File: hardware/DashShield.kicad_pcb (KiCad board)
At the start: 2 copper layers, 95 parts, among them J1 GPIO, J2 Steering Wheel, J3 Dash LEDs, J4 CAN0, J5 PWR, J7 CAN1, Q1 2N7002, Q2 2N7002, Q3 2N7002, Q4 2N7002, Q5 2N7002, Q6 2N7002, Q7 2N7002, Q8 2N7002, Q9 2N7002, U1 CAT24C256, U2 MCP2562-E-SN, U3 MCP2515-xST, U4 MCP2515-xST, U5 MCP2562-E-SN, Y1 8MHz, Y2 8MHz

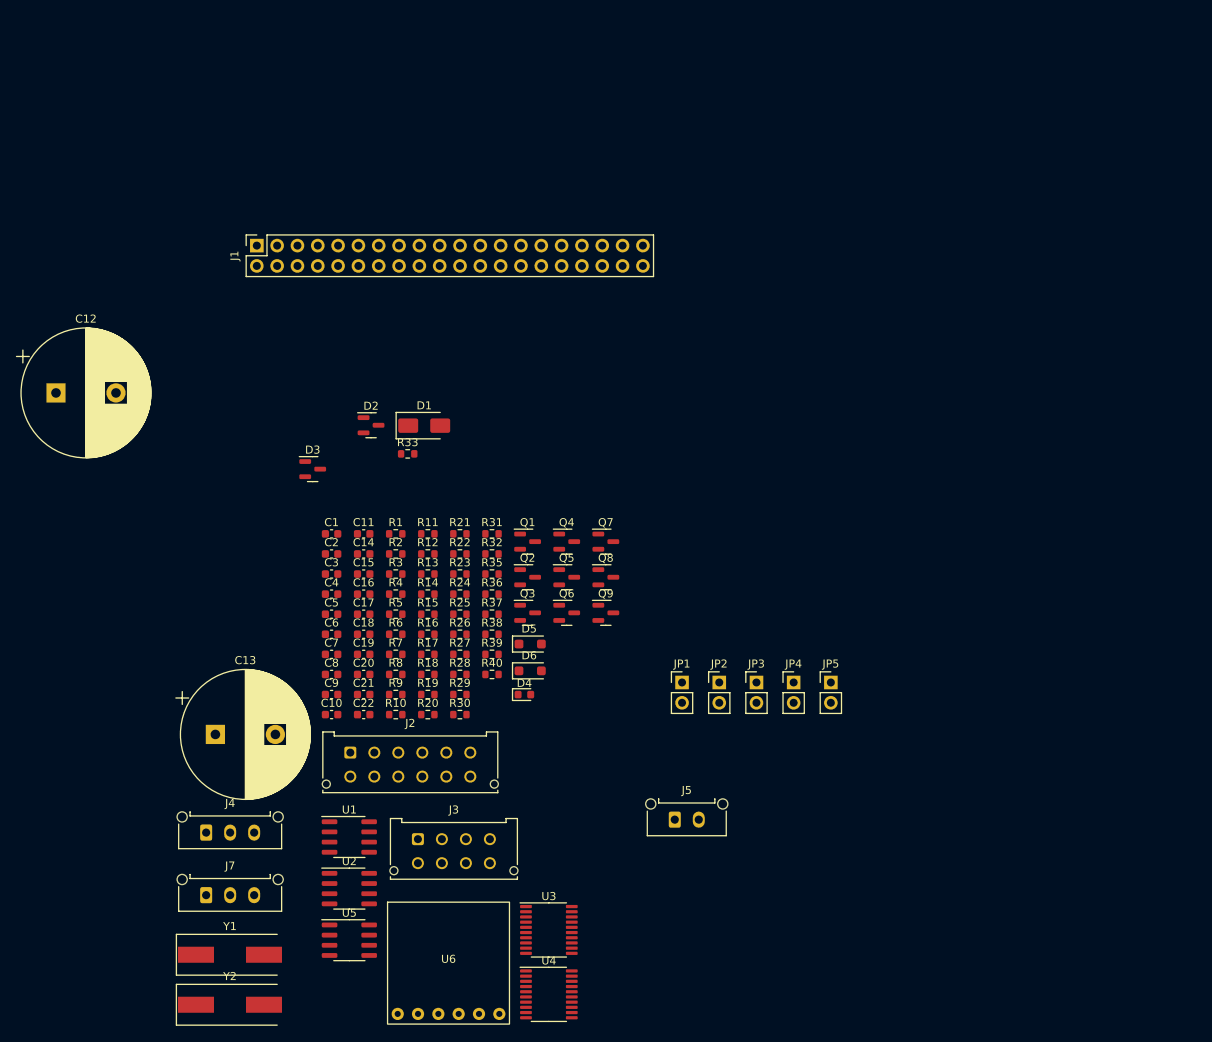
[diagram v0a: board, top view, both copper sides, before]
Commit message: feat: update steering wheel interface to 5V <-> 3.3V logic
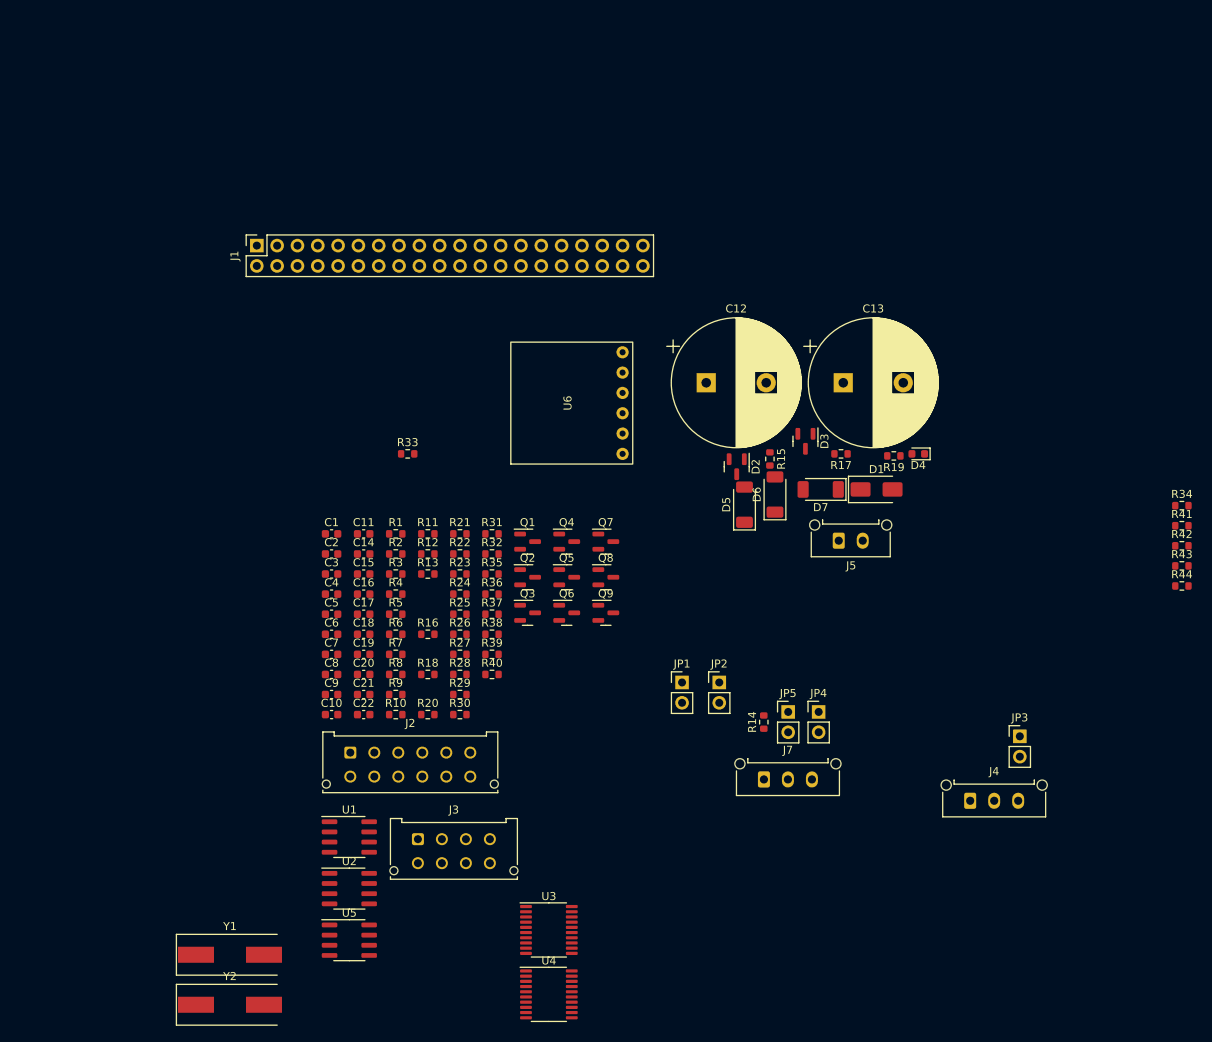
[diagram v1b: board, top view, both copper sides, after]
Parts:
- added D7: PMEG3050, Diode_SMD:D_SOD-128, F.Cu at (134.6, 112.4)
- added R34: 10k, Resistor_SMD:R_0603_1608Metric, F.Cu at (179.8, 114.4)
- added R41: 10k, Resistor_SMD:R_0603_1608Metric, F.Cu at (179.8, 116.9)
- added R42: 10k, Resistor_SMD:R_0603_1608Metric, F.Cu at (179.8, 119.4)
- added R43: 500, Resistor_SMD:R_0603_1608Metric, F.Cu at (179.8, 122.0)
- added R44: 1k, Resistor_SMD:R_0603_1608Metric, F.Cu at (179.8, 124.5)
- D5, D6: value CRS15 -> PMEG3050; footprint Diode_SMD:D_SOD-123F -> Diode_SMD:D_SOD-128
- R1, R2: value 3.9k -> 3k9
- R29: value 1k -> 500
- R35, R37, R39: value 10k -> 20k
- moved J4 95.6 mm to (153.3, 151.3)
- moved C13 90.0 mm to (137.4, 99.1)
- moved C12 81.3 mm to (120.3, 99.1)
- moved U6 71.7 mm to (103.5, 101.6), turned to 90 degrees
- moved J7 71.2 mm to (127.5, 148.6)
- moved R19 65.4 mm to (143.8, 108.2), turned to 180 degrees
- moved D3 61.7 mm to (132.7, 106.4), turned to -90 degrees
- moved D4 57.7 mm to (146.8, 108.0), turned to 180 degrees
- moved R17 57.4 mm to (137.2, 108.0), turned to 180 degrees
- moved D1 57.1 mm to (141.6, 112.4)
- moved R15 47.0 mm to (128.3, 108.6), turned to -90 degrees
- moved D2 46.0 mm to (124.1, 109.6), turned to -90 degrees
- moved R14 44.9 mm to (127.5, 141.5), turned to 90 degrees
- moved J5 40.4 mm to (136.9, 118.8)
- moved D6 37.7 mm to (128.9, 113.0), turned to 90 degrees
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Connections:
- J2 pad 7: +3.3V -> +5V
- J5 pad 1: VS -> Net-(D7-A)
- R29 pad 2: GND -> Net-(R29-Pad2)
- R30 pad 1: /TC Power Adjust Dial -> Net-(R29-Pad2)
- R31 pad 2: /Wheel Slip Adjust Dial -> Net-(R29-Pad2)
- R32 pad 2: /TC Power Adjust Dial -> Net-(R32-Pad2)
- R35 pad 1: /Lap Marker Button -> Net-(R35-Pad1)
- R36 pad 2: /Lap Marker Button -> Net-(R35-Pad1)
- R37 pad 1: /Radio Enable Button -> Net-(R37-Pad1)
- R38 pad 2: /Radio Enable Button -> Net-(R37-Pad1)
- R39 pad 1: /TC Disable Button -> Net-(R34-Pad2)
- R40 pad 2: /TC Disable Button -> Net-(R34-Pad2)

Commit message: fix: apply Ayden's design review
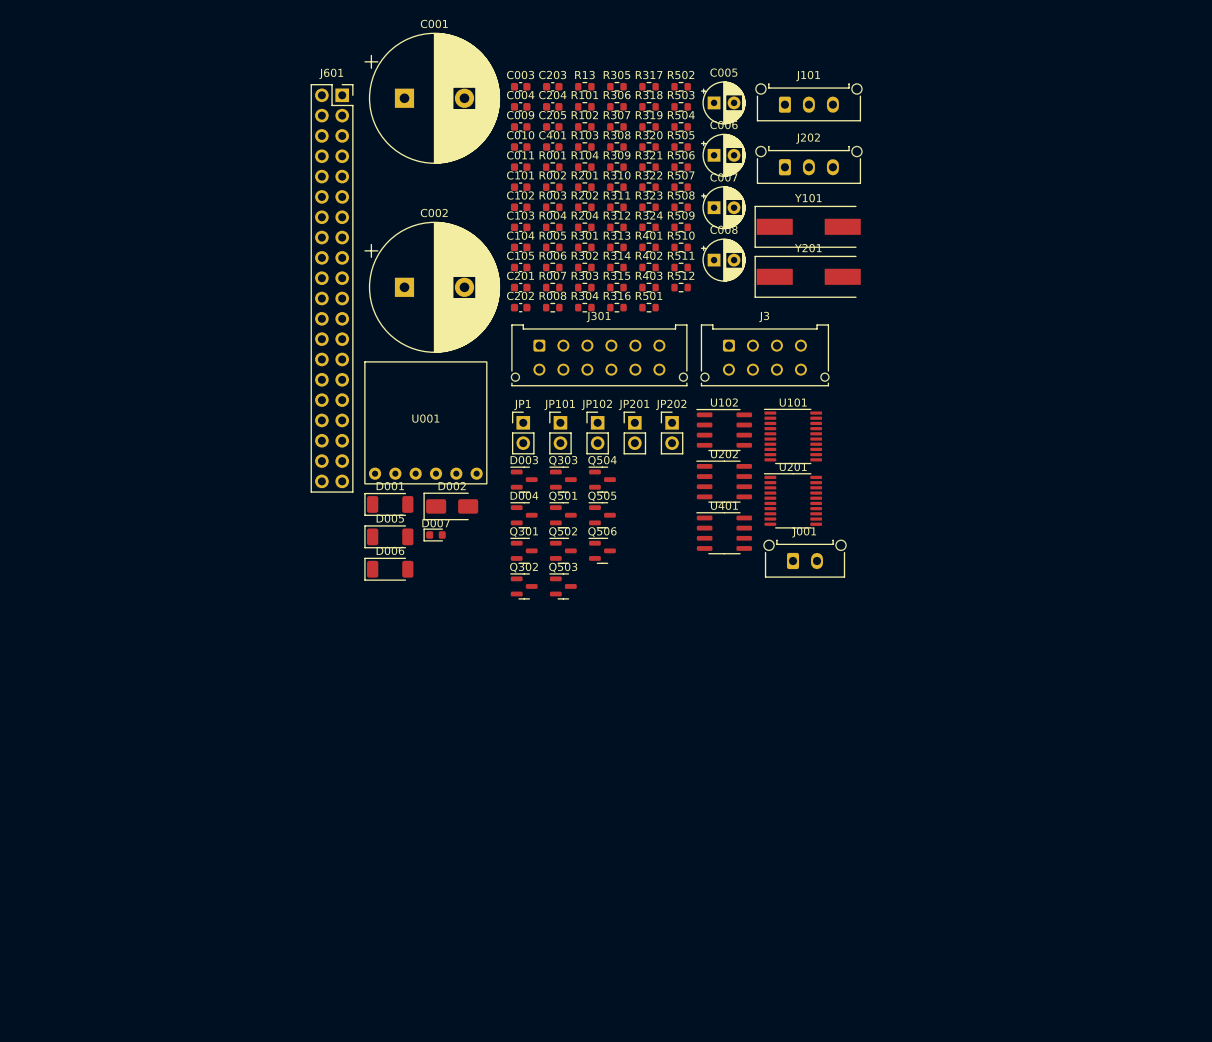
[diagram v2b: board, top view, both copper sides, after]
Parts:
- removed C1: 100n, Capacitor_SMD:C_0603_1608Metric
- removed C10, C11, C17, C18, C2, C3, C6, C7: 100nF, Capacitor_SMD:C_0603_1608Metric
- removed C12, C13: 25F, Capacitor_THT:CP_Radial_D16.0mm_P7.50mm
- removed C14, C15, C16, C19: 10uF, Capacitor_SMD:C_0603_1608Metric
- removed C20, C21, C22: 10nF, Capacitor_SMD:C_0603_1608Metric
- removed C4, C5, C8, C9: 22pF, Capacitor_SMD:C_0603_1608Metric
- removed D1: 5.1V, Diode_SMD:D_SMA
- removed D2, D3: 2.7V, Package_TO_SOT_SMD:SOT-23
- removed D4: LED, LED_SMD:LED_0603_1608Metric
- removed D5, D6, D7: PMEG3050, Diode_SMD:D_SOD-128
- removed J1: GPIO, Connector_PinSocket_2.54mm:PinSocket_2x20_P2.54mm_Vertical
- removed J2: Steering Wheel, Connector_Molex:Molex_Micro-Fit_3.0_43045-1212_2x06_P3.00mm_Vertical
- removed J4: CAN0, Connector_Molex:Molex_Micro-Fit_3.0_43650-0315_1x03_P3.00mm_Vertical
- removed J5: PWR, Connector_Molex:Molex_Micro-Fit_3.0_43650-0215_1x02_P3.00mm_Vertical
- removed J7: CAN1, Connector_Molex:Molex_Micro-Fit_3.0_43650-0315_1x03_P3.00mm_Vertical
- removed JP2, JP5: Termination Jumper, Connector_PinHeader_2.54mm:PinHeader_1x02_P2.54mm_Vertical
- removed JP3, JP4: Shielding Jumper, Connector_PinHeader_2.54mm:PinHeader_1x02_P2.54mm_Vertical
- removed Q1, Q2, Q3, Q4, Q5, Q6, Q7, Q8, Q9: 2N7002, Package_TO_SOT_SMD:SOT-23
- removed R1, R2: 3k9, Resistor_SMD:R_0603_1608Metric
- removed R10, R12: 0, Resistor_SMD:R_0603_1608Metric
- removed R11: 4k7, Resistor_SMD:R_0603_1608Metric
- removed R14, R9: 120, Resistor_SMD:R_0603_1608Metric
- removed R15, R17, R19, R30, R33, R44: 1k, Resistor_SMD:R_0603_1608Metric
- removed R16: 3.3, Resistor_SMD:R_0603_1608Metric
- removed R18, R22, R35, R37, R39: 20k, Resistor_SMD:R_0603_1608Metric
- removed R20, R21, R31, R32, R34, R36, R38, R40, R41, R42: 10k, Resistor_SMD:R_0603_1608Metric
- removed R23, R24, R25, R26, R27, R28, R3, R4, R5, R6, R7, R8: 270, Resistor_SMD:R_0603_1608Metric
- removed R29, R43: 500, Resistor_SMD:R_0603_1608Metric
- removed U1: CAT24C256, Package_SO:SOIC-8_3.9x4.9mm_P1.27mm
- removed U2, U5: MCP2562-E-SN, Package_SO:SOIC-8_3.9x4.9mm_P1.27mm
- removed U3, U4: MCP2515-xST, Package_SO:TSSOP-20_4.4x6.5mm_P0.65mm
- removed U6: ~, U3V40x:U3V40x
- removed Y1, Y2: 8MHz, Crystal:Crystal_SMD_HC49-SD
- added C001: 25F, Capacitor_THT:CP_Radial_D16.0mm_P7.50mm, F.Cu at (82.6, 63.5)
- added C002: 25F, Capacitor_THT:CP_Radial_D16.0mm_P7.50mm, F.Cu at (82.6, 87.1)
- added C003: 10nF, Capacitor_SMD:C_0603_1608Metric, F.Cu at (97.1, 62.1)
- added C004: 10nF, Capacitor_SMD:C_0603_1608Metric, F.Cu at (97.1, 64.6)
- added C005: 10uF, Capacitor_THT:CP_Radial_D5.0mm_P2.50mm, F.Cu at (121.3, 64.1)
- added C006: 100uF, Capacitor_THT:CP_Radial_D5.0mm_P2.50mm, F.Cu at (121.3, 70.6)
- added C007: 10uF, Capacitor_THT:CP_Radial_D5.0mm_P2.50mm, F.Cu at (121.3, 77.2)
- added C008: 10uF, Capacitor_THT:CP_Radial_D5.0mm_P2.50mm, F.Cu at (121.3, 83.7)
- added C009: 100nF, Capacitor_SMD:C_0603_1608Metric, F.Cu at (97.1, 67.1)
- added C010: 100nF, Capacitor_SMD:C_0603_1608Metric, F.Cu at (97.1, 69.6)
- added C011: 10nF, Capacitor_SMD:C_0603_1608Metric, F.Cu at (97.1, 72.1)
- added C101: 100nF, Capacitor_SMD:C_0603_1608Metric, F.Cu at (97.1, 74.6)
- added C102: 22pF, Capacitor_SMD:C_0603_1608Metric, F.Cu at (97.1, 77.1)
- added C103: 22pF, Capacitor_SMD:C_0603_1608Metric, F.Cu at (97.1, 79.6)
- added C104: 100nF, Capacitor_SMD:C_0603_1608Metric, F.Cu at (97.1, 82.1)
- added C105: 100nF, Capacitor_SMD:C_0603_1608Metric, F.Cu at (97.1, 84.7)
- added C201: 100nF, Capacitor_SMD:C_0603_1608Metric, F.Cu at (97.1, 87.2)
- added C202: 22pF, Capacitor_SMD:C_0603_1608Metric, F.Cu at (97.1, 89.7)
- added C203: 22pF, Capacitor_SMD:C_0603_1608Metric, F.Cu at (101.1, 62.1)
- added C204: 100nF, Capacitor_SMD:C_0603_1608Metric, F.Cu at (101.1, 64.6)
- added C205: 100nF, Capacitor_SMD:C_0603_1608Metric, F.Cu at (101.1, 67.1)
- added C401: 100nF, Capacitor_SMD:C_0603_1608Metric, F.Cu at (101.1, 69.6)
- added D001: PMEG3050, Diode_SMD:D_SOD-128, F.Cu at (80.8, 114.3)
- added D002: 5.1V, Diode_SMD:D_SMA, F.Cu at (88.6, 114.5)
- added D003: 2.7V, Package_TO_SOT_SMD:SOT-23, F.Cu at (97.6, 111.2)
- added D004: 2.7V, Package_TO_SOT_SMD:SOT-23, F.Cu at (97.6, 115.6)
- added D005: PMEG3050, Diode_SMD:D_SOD-128, F.Cu at (80.8, 118.3)
- added D006: PMEG3050, Diode_SMD:D_SOD-128, F.Cu at (80.8, 122.4)
- added D007: LED, LED_SMD:LED_0603_1608Metric, F.Cu at (86.5, 118.1)
- added J001: PWR, Connector_Molex:Molex_Micro-Fit_3.0_43650-0215_1x02_P3.00mm_Vertical, F.Cu at (131.2, 121.3)
- added J101: CAN0, Connector_Molex:Molex_Micro-Fit_3.0_43650-0315_1x03_P3.00mm_Vertical, F.Cu at (130.2, 64.3)
- added J202: CAN1, Connector_Molex:Molex_Micro-Fit_3.0_43650-0315_1x03_P3.00mm_Vertical, F.Cu at (130.2, 72.1)
- added J301: Steering Wheel, Connector_Molex:Molex_Micro-Fit_3.0_43045-1212_2x06_P3.00mm_Vertical, F.Cu at (99.5, 94.4)
- added J601: GPIO, Connector_PinSocket_2.54mm:PinSocket_2x20_P2.54mm_Vertical, F.Cu at (74.8, 63.1)
- added JP101: Termination Jumper, Connector_PinHeader_2.54mm:PinHeader_1x02_P2.54mm_Vertical, F.Cu at (102.1, 104.1)
- added JP102: Shielding Jumper, Connector_PinHeader_2.54mm:PinHeader_1x02_P2.54mm_Vertical, F.Cu at (106.7, 104.1)
- added JP201: Termination Jumper, Connector_PinHeader_2.54mm:PinHeader_1x02_P2.54mm_Vertical, F.Cu at (111.4, 104.1)
- added JP202: Shielding Jumper, Connector_PinHeader_2.54mm:PinHeader_1x02_P2.54mm_Vertical, F.Cu at (116.0, 104.1)
- added Q301: 2N7002, Package_TO_SOT_SMD:SOT-23, F.Cu at (97.6, 120.1)
- added Q302: 2N7002, Package_TO_SOT_SMD:SOT-23, F.Cu at (97.6, 124.5)
- added Q303: 2N7002, Package_TO_SOT_SMD:SOT-23, F.Cu at (102.5, 111.2)
- added Q501: 2N7002, Package_TO_SOT_SMD:SOT-23, F.Cu at (102.5, 115.6)
- added Q502: 2N7002, Package_TO_SOT_SMD:SOT-23, F.Cu at (102.5, 120.1)
- added Q503: 2N7002, Package_TO_SOT_SMD:SOT-23, F.Cu at (102.5, 124.5)
- added Q504: 2N7002, Package_TO_SOT_SMD:SOT-23, F.Cu at (107.3, 111.2)
- added Q505: 2N7002, Package_TO_SOT_SMD:SOT-23, F.Cu at (107.3, 115.6)
- added Q506: 2N7002, Package_TO_SOT_SMD:SOT-23, F.Cu at (107.3, 120.1)
- added R001: 3.3, Resistor_SMD:R_0603_1608Metric, F.Cu at (101.1, 72.1)
- added R002: 1k, Resistor_SMD:R_0603_1608Metric, F.Cu at (101.1, 74.6)
- added R003: 1k, Resistor_SMD:R_0603_1608Metric, F.Cu at (101.1, 77.1)
- added R004: 1k, Resistor_SMD:R_0603_1608Metric, F.Cu at (101.1, 79.6)
- added R005: 10k, Resistor_SMD:R_0603_1608Metric, F.Cu at (101.1, 82.1)
- added R006: 20k, Resistor_SMD:R_0603_1608Metric, F.Cu at (101.1, 84.7)
- added R007: 10k, Resistor_SMD:R_0603_1608Metric, F.Cu at (101.1, 87.2)
- added R008: 20k, Resistor_SMD:R_0603_1608Metric, F.Cu at (101.1, 89.7)
- added R101: 0, Resistor_SMD:R_0603_1608Metric, F.Cu at (105.1, 64.6)
- added R102: 0, Resistor_SMD:R_0603_1608Metric, F.Cu at (105.1, 67.1)
- added R103: 4k7, Resistor_SMD:R_0603_1608Metric, F.Cu at (105.1, 69.6)
- added R104: 120, Resistor_SMD:R_0603_1608Metric, F.Cu at (105.1, 72.1)
- added R201: 0, Resistor_SMD:R_0603_1608Metric, F.Cu at (105.1, 74.6)
- added R202: 0, Resistor_SMD:R_0603_1608Metric, F.Cu at (105.1, 77.1)
- added R204: 120, Resistor_SMD:R_0603_1608Metric, F.Cu at (105.1, 79.6)
- added R301: 10k, Resistor_SMD:R_0603_1608Metric, F.Cu at (105.1, 82.1)
- added R302: 20k, Resistor_SMD:R_0603_1608Metric, F.Cu at (105.1, 84.7)
- added R303: 10k, Resistor_SMD:R_0603_1608Metric, F.Cu at (105.1, 87.2)
- added R304: 10k, Resistor_SMD:R_0603_1608Metric, F.Cu at (105.1, 89.7)
- added R305: 20k, Resistor_SMD:R_0603_1608Metric, F.Cu at (109.2, 62.1)
- added R306: 10k, Resistor_SMD:R_0603_1608Metric, F.Cu at (109.2, 64.6)
- added R307: 10k, Resistor_SMD:R_0603_1608Metric, F.Cu at (109.2, 67.1)
- added R308: 20k, Resistor_SMD:R_0603_1608Metric, F.Cu at (109.2, 69.6)
- added R309: 10k, Resistor_SMD:R_0603_1608Metric, F.Cu at (109.2, 72.1)
- added R310: 500, Resistor_SMD:R_0603_1608Metric, F.Cu at (109.2, 74.6)
- added R311: 1k, Resistor_SMD:R_0603_1608Metric, F.Cu at (109.2, 77.1)
- added R312: 10k, Resistor_SMD:R_0603_1608Metric, F.Cu at (109.2, 79.6)
- added R313: 500, Resistor_SMD:R_0603_1608Metric, F.Cu at (109.2, 82.1)
- added R314: 1k, Resistor_SMD:R_0603_1608Metric, F.Cu at (109.2, 84.7)
- added R315: 10k, Resistor_SMD:R_0603_1608Metric, F.Cu at (109.2, 87.2)
- added R316: 270, Resistor_SMD:R_0603_1608Metric, F.Cu at (109.2, 89.7)
- added R317: 270, Resistor_SMD:R_0603_1608Metric, F.Cu at (113.2, 62.1)
- added R318: 10k, Resistor_SMD:R_0603_1608Metric, F.Cu at (113.2, 64.6)
- added R319: 270, Resistor_SMD:R_0603_1608Metric, F.Cu at (113.2, 67.1)
- added R320: 270, Resistor_SMD:R_0603_1608Metric, F.Cu at (113.2, 69.6)
- added R321: 10k, Resistor_SMD:R_0603_1608Metric, F.Cu at (113.2, 72.1)
- added R322: 270, Resistor_SMD:R_0603_1608Metric, F.Cu at (113.2, 74.6)
- added R323: 270, Resistor_SMD:R_0603_1608Metric, F.Cu at (113.2, 77.1)
- added R324: 10k, Resistor_SMD:R_0603_1608Metric, F.Cu at (113.2, 79.6)
- added R401: 3k9, Resistor_SMD:R_0603_1608Metric, F.Cu at (113.2, 82.1)
- added R402: 3k9, Resistor_SMD:R_0603_1608Metric, F.Cu at (113.2, 84.7)
- added R403: 1k, Resistor_SMD:R_0603_1608Metric, F.Cu at (113.2, 87.2)
- added R501: 270, Resistor_SMD:R_0603_1608Metric, F.Cu at (113.2, 89.7)
- added R502: 10k, Resistor_SMD:R_0603_1608Metric, F.Cu at (117.2, 62.1)
- added R503: 270, Resistor_SMD:R_0603_1608Metric, F.Cu at (117.2, 64.6)
- added R504: 10k, Resistor_SMD:R_0603_1608Metric, F.Cu at (117.2, 67.1)
- added R505: 270, Resistor_SMD:R_0603_1608Metric, F.Cu at (117.2, 69.6)
- added R506: 10k, Resistor_SMD:R_0603_1608Metric, F.Cu at (117.2, 72.1)
- added R507: 270, Resistor_SMD:R_0603_1608Metric, F.Cu at (117.2, 74.6)
- added R508: 10k, Resistor_SMD:R_0603_1608Metric, F.Cu at (117.2, 77.1)
- added R509: 270, Resistor_SMD:R_0603_1608Metric, F.Cu at (117.2, 79.6)
- added R510: 10k, Resistor_SMD:R_0603_1608Metric, F.Cu at (117.2, 82.1)
- added R511: 270, Resistor_SMD:R_0603_1608Metric, F.Cu at (117.2, 84.7)
- added R512: 10k, Resistor_SMD:R_0603_1608Metric, F.Cu at (117.2, 87.2)
- added U001: ~, U3V40x:U3V40x, F.Cu at (85.3, 104.1)
- added U101: MCP2515-xST, Package_SO:TSSOP-20_4.4x6.5mm_P0.65mm, F.Cu at (131.2, 105.8)
- added U102: MCP2562-E-SN, Package_SO:SOIC-8_3.9x4.9mm_P1.27mm, F.Cu at (122.6, 105.0)
- added U201: MCP2515-xST, Package_SO:TSSOP-20_4.4x6.5mm_P0.65mm, F.Cu at (131.2, 113.8)
- added U202: MCP2562-E-SN, Package_SO:SOIC-8_3.9x4.9mm_P1.27mm, F.Cu at (122.6, 111.4)
- added U401: CAT24C256, Package_SO:SOIC-8_3.9x4.9mm_P1.27mm, F.Cu at (122.6, 117.9)
- added Y101: 8MHz, Crystal:Crystal_SMD_HC49-SD, F.Cu at (133.1, 79.6)
- added Y201: 8MHz, Crystal:Crystal_SMD_HC49-SD, F.Cu at (133.1, 85.8)
- moved J3 72.9 mm to (123.2, 94.4)
- moved R13 64.0 mm to (105.1, 62.1)
- moved JP1 38.0 mm to (97.4, 104.1)
